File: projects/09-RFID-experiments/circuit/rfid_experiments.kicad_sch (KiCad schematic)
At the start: 5 parts, among them SW2 SW_MEC_5E

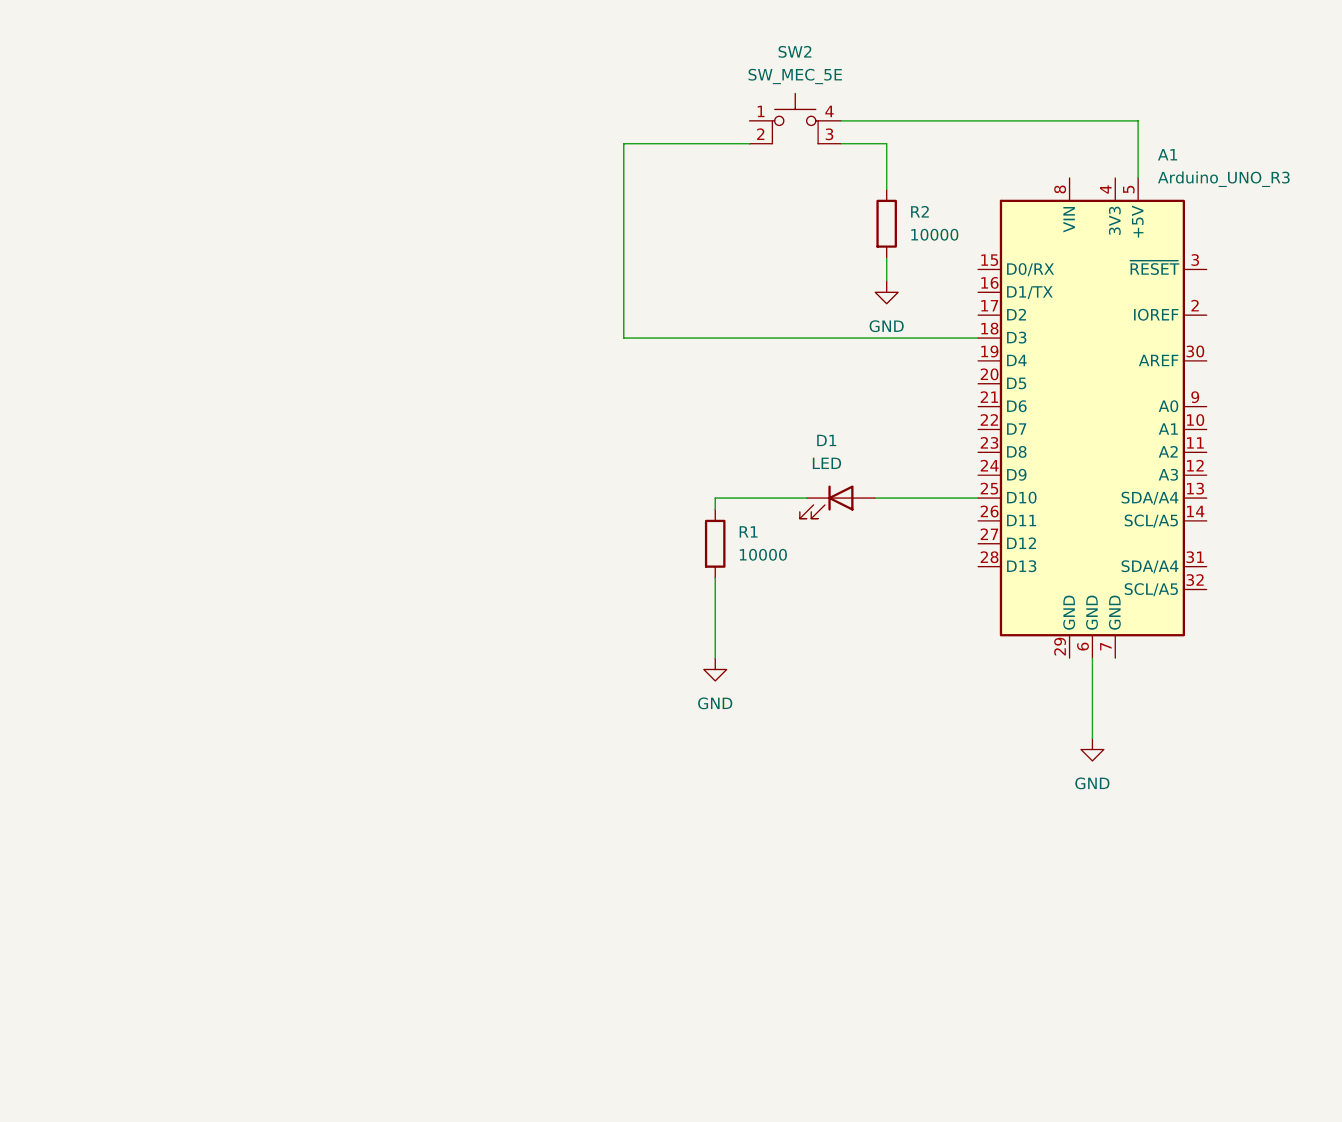
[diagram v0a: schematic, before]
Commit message: FEAT add circuit schema and RFID-RC522 library
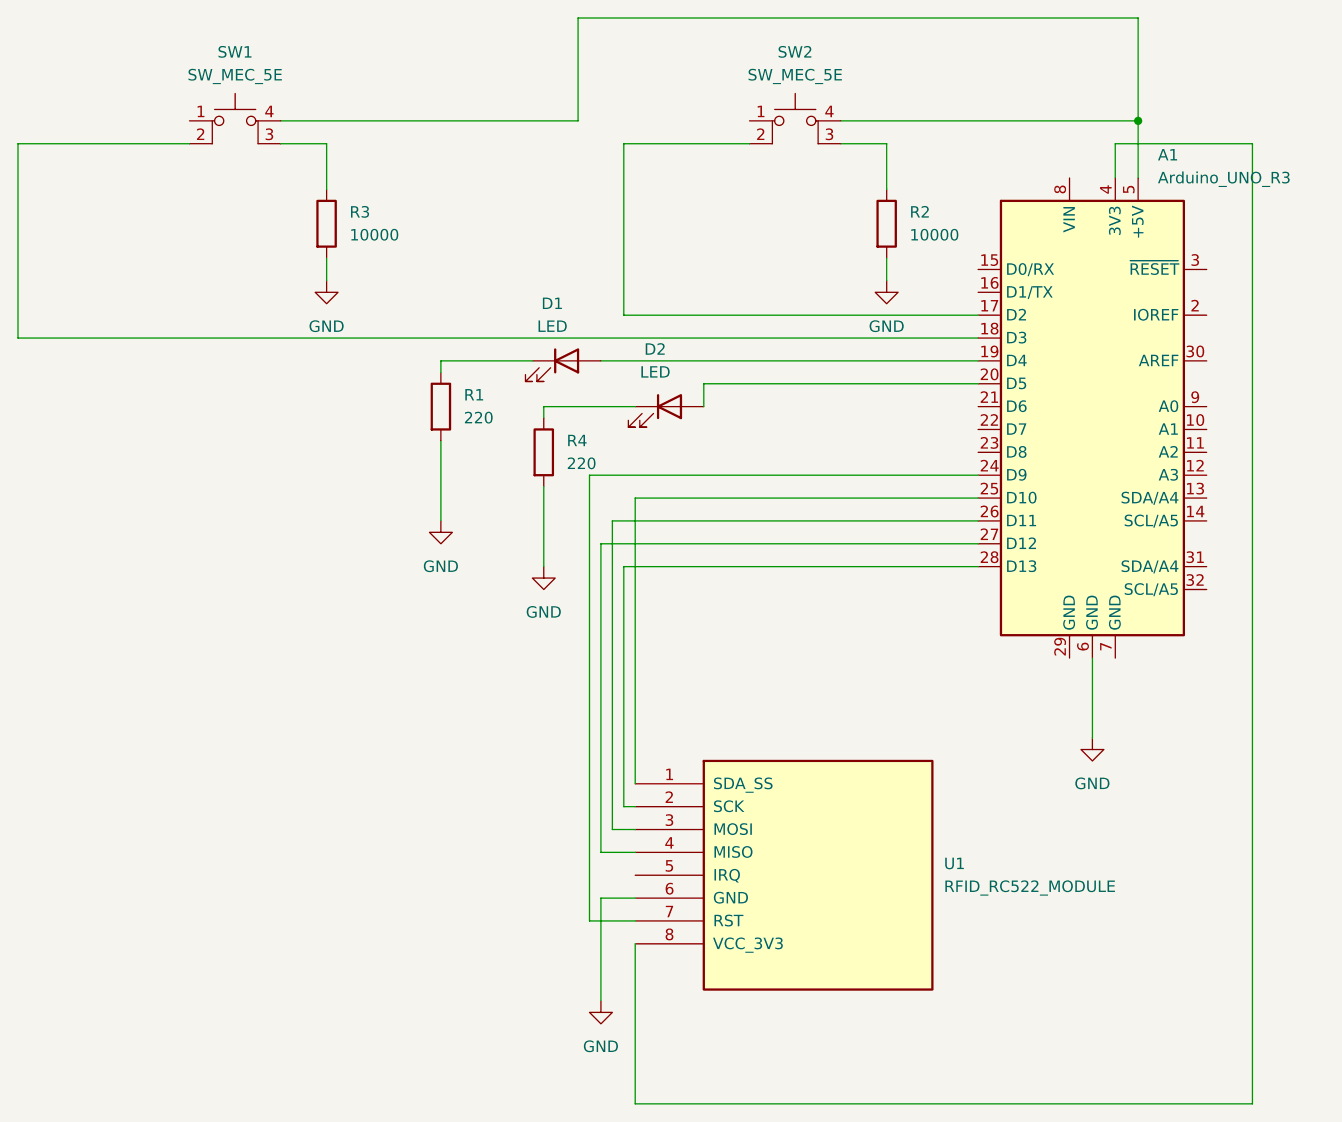
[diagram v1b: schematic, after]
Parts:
- added D2: LED, symbol Device:LED
- added R3: 10000, symbol Device:R
- added R4: 220, symbol Device:R
- added SW1: SW_MEC_5E, symbol Switch:SW_MEC_5E
- added U1: RFID_RC522_MODULE, symbol RFID-RC522:RFID_RC522_MODULE
- R1: value 10000 -> 220
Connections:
- net GND: now also R3.2, R4.2, U1.6 (GND)
- net at D1.2 (A): now also A1.19 (D4); no longer A1.25 (D10)
- net at SW2.2: now also A1.17 (D2); no longer A1.18 (D3)
- net at A1.5 (+5V), SW2.4 (A): now also SW1.4 (A)
- net at A1.20 (D5): now also D2.2 (A)
- net at A1.24 (D9): now also U1.7 (RST)
- net at A1.26 (D11): now also U1.3 (MOSI)
- net at A1.27 (D12): now also U1.4 (MISO)
- net at A1.28 (D13): now also U1.2 (SCK)
- net at A1.4 (3V3): now also U1.8 (VCC_3V3)
- new net: D2.1 (K), R4.1
- new net: A1.18 (D3), SW1.2
- new net: A1.25 (D10), U1.1 (SDA_SS)
- new net: R3.1, SW1.3 (K)
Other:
- moved on the sheet: D1, R1
